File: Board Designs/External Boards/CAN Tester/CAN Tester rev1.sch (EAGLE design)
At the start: 25 parts, among them M1 Minifit, M2 Nanofit, U1 ISOLATED CAN TERMINAL, U2 TERMINATION_RESISTOR_JUMPER, U3 TEENSY_3.2_SIMPLE, U4 CHARACTER_LCD

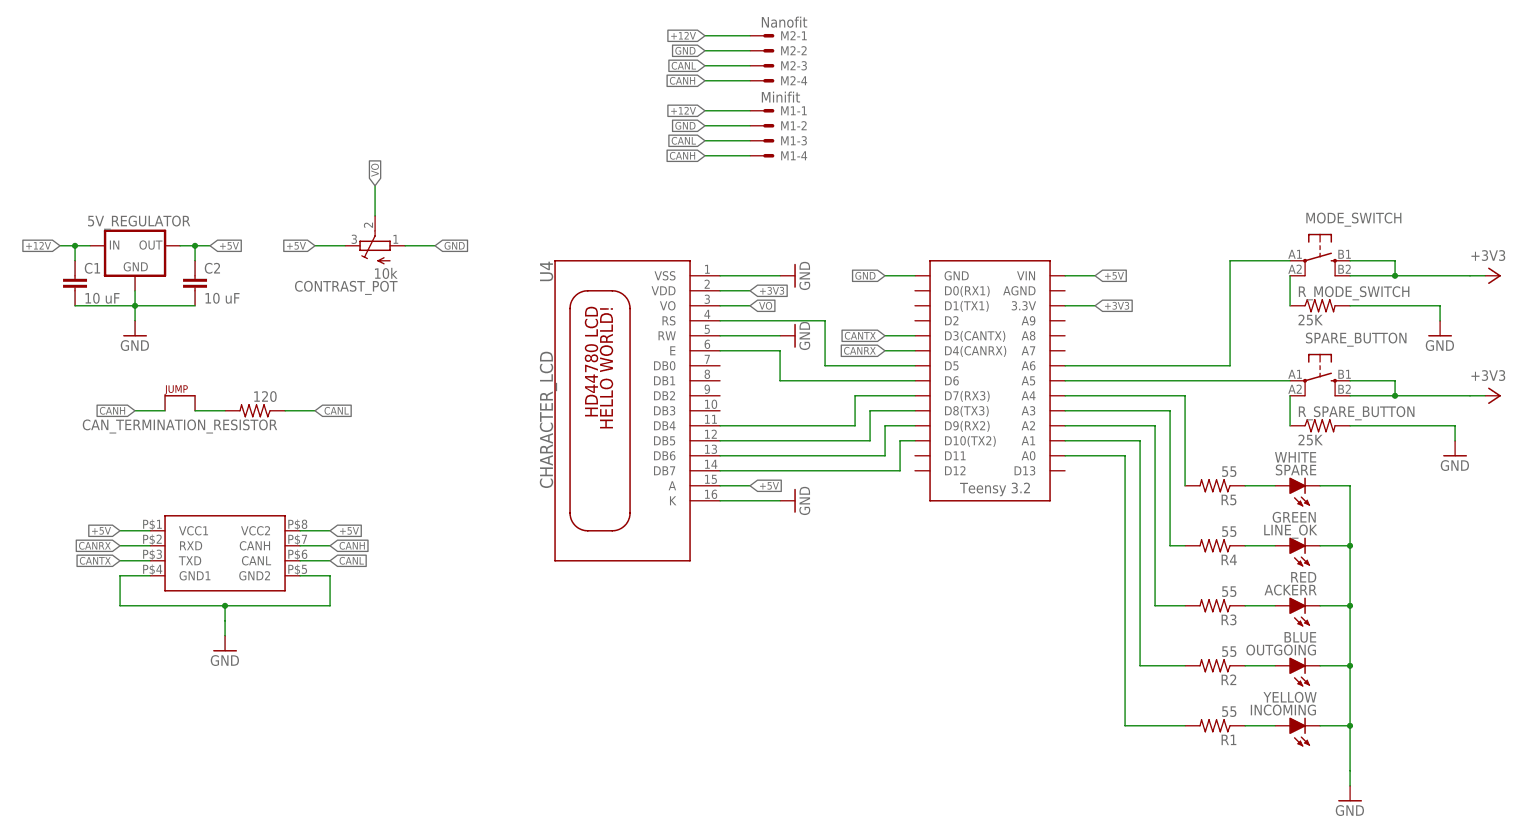
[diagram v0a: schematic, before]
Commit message: Moved the location of the can tester folder.
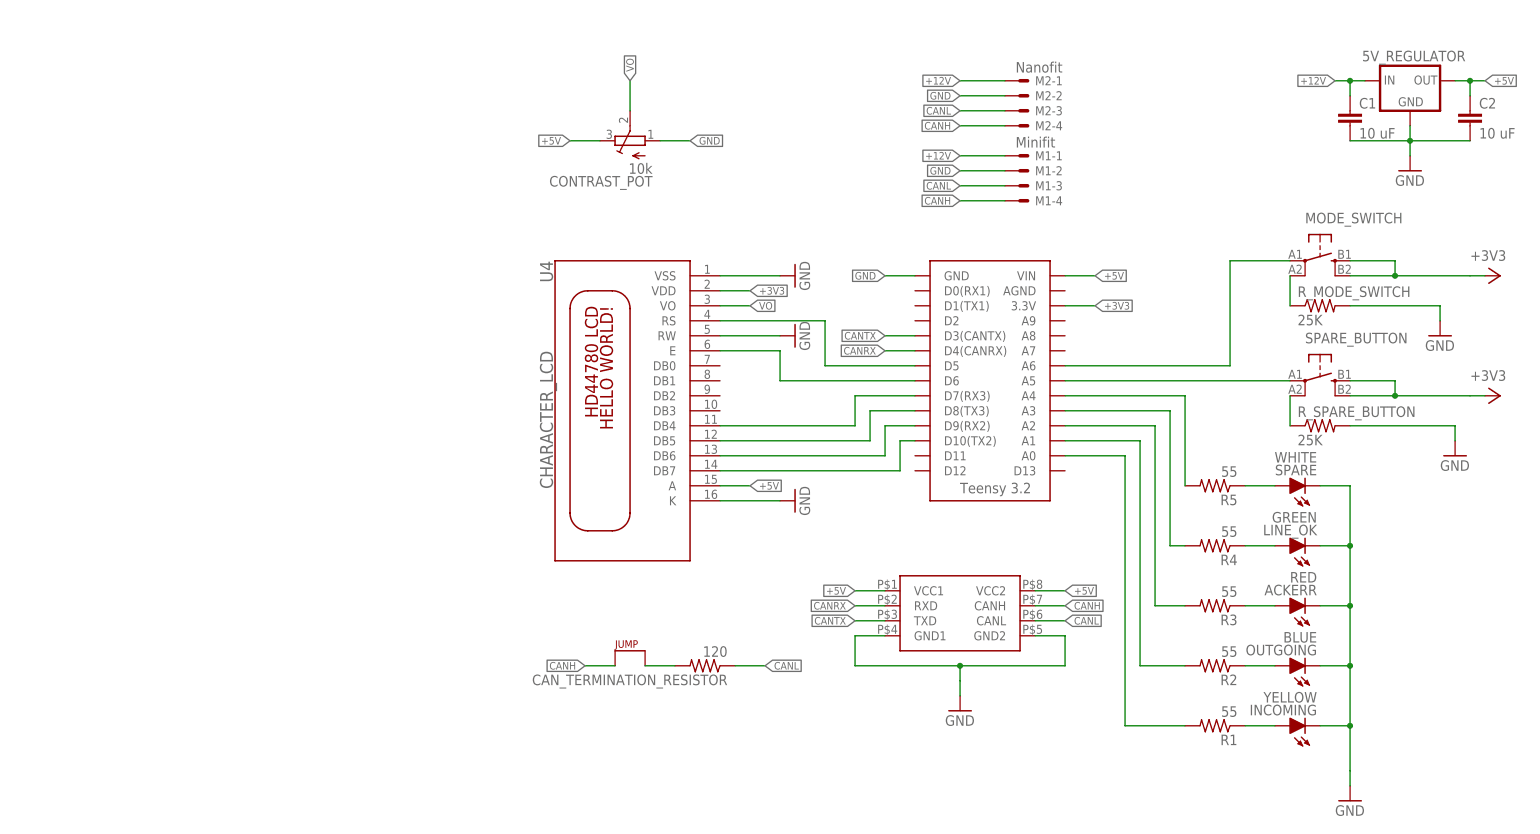
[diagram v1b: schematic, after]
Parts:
- U1: value ISOLATED CAN TERMINAL -> ISOLATED CAN TRANSCIEVER
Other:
- moved on the sheet: 5V_REGULATOR, C1, C2, CAN_TERMINATION_RESISTOR, CONTRAST_POT, M1-1, M1-2, M1-3, M1-4, M2-1, M2-2, M2-3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

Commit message: Verified schematic, but had to restart board
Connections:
- removed net N$15: R_MODE_SWITCH.2
- net GND: now also R_MODE_SWITCH.2
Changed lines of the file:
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@@
 <setting verticaltext="up"/>
 </settings>
-<grid distance="0.1" unitdist="inch" unit="inch" style="dots" multiple="1" display="yes" altdistance="0.01" altunitdist="inch" altunit="inch"/>
+<grid distance="0.1" unitdist="inch" unit="inch" style="lines" multiple="1" display="yes" altdistance="0.01" altunitdist="inch" altunit="inch"/>
 <layers>
 <layer number="1" name="Top" color="4" fill="1" visible="no" active="no"/>
@@
 </variantdefs>
 <classes>
-<class number="0" name="default" width="0" drill="0">
+<class number="0" name="default" width="0.762" drill="0">
+<clearance class="0" value="0.381"/>
 </class>
 </classes>
@@
 </segment>
 <segment>
-<pinref part="R_SPARE_BUTTON" gate="G$1" pin="2"/>
-<wire x1="167.64" y1="40.64" x2="185.42" y2="40.64" width="0.1524" layer="91"/>
-<pinref part="GND3" gate="1" pin="GND"/>
-<wire x1="185.42" y1="40.64" x2="185.42" y2="38.1" width="0.1524" layer="91"/>
-</segment>
-<segment>
-<pinref part="GND4" gate="1" pin="GND"/>
-<wire x1="182.88" y1="60.96" x2="182.88" y2="58.42" width="0.1524" layer="91"/>
-</segment>
-<segment>
 <pinref part="GND5" gate="1" pin="GND"/>
 <wire x1="101.6" y1="-5.08" x2="101.6" y2="-2.54" width="0.1524" layer="91"/>
@@
 <wire x1="109.22" y1="83.82" x2="101.6" y2="83.82" width="0.1524" layer="91"/>
 <label x="101.6" y="83.82" size="1.27" layer="95" rot="R180" xref="yes"/>
+</segment>
+<segment>
+<pinref part="R_SPARE_BUTTON" gate="G$1" pin="2"/>
+<pinref part="GND3" gate="1" pin="GND"/>
+<wire x1="167.64" y1="40.64" x2="185.42" y2="40.64" width="0.1524" layer="91"/>
+<wire x1="185.42" y1="40.64" x2="185.42" y2="38.1" width="0.1524" layer="91"/>
+</segment>
+<segment>
+<pinref part="GND4" gate="1" pin="GND"/>
+<wire x1="182.88" y1="58.42" x2="182.88" y2="60.96" width="0.1524" layer="91"/>
+<pinref part="R_MODE_SWITCH" gate="G$1" pin="2"/>
+<wire x1="182.88" y1="60.96" x2="167.64" y2="60.96" width="0.1524" layer="91"/>
 </segment>
 </net>
@@
 <pinref part="SPARE_BUTTON" gate="1" pin="P"/>
 <wire x1="119.38" y1="48.26" x2="157.48" y2="48.26" width="0.1524" layer="91"/>
-</segment>
-</net>
-<net name="N$12" class="0">
-<segment>
-<pinref part="SPARE_BUTTON" gate="1" pin="P1"/>
-<pinref part="R_SPARE_BUTTON" gate="G$1" pin="1"/>
-<wire x1="157.48" y1="45.72" x2="157.48" y2="40.64" width="0.1524" layer="91"/>
 </segment>
 </net>
@@
 <pinref part="MODE_SWITCH" gate="1" pin="P"/>
 <wire x1="147.32" y1="68.58" x2="157.48" y2="68.58" width="0.1524" layer="91"/>
-</segment>
-</net>
-<net name="N$14" class="0">
-<segment>
-<pinref part="MODE_SWITCH" gate="1" pin="P1"/>
-<pinref part="R_MODE_SWITCH" gate="G$1" pin="1"/>
-<wire x1="157.48" y1="66.04" x2="157.48" y2="60.96" width="0.1524" layer="91"/>
-</segment>
-</net>
-<net name="N$15" class="0">
-<segment>
-<pinref part="R_MODE_SWITCH" gate="G$1" pin="2"/>
-<wire x1="167.64" y1="60.96" x2="182.88" y2="60.96" width="0.1524" layer="91"/>
 </segment>
 </net>
@@
 </segment>
 </net>
+<net name="N$12" class="0">
+<segment>
+<pinref part="MODE_SWITCH" gate="1" pin="P1"/>
+<pinref part="R_MODE_SWITCH" gate="G$1" pin="1"/>
+<wire x1="157.48" y1="66.04" x2="157.48" y2="60.96" width="0.1524" layer="91"/>
+</segment>
+</net>
+<net name="N$14" class="0">
+<segment>
+<pinref part="SPARE_BUTTON" gate="1" pin="P1"/>
+<pinref part="R_SPARE_BUTTON" gate="G$1" pin="1"/>
+<wire x1="157.48" y1="45.72" x2="157.48" y2="40.64" width="0.1524" layer="91"/>
+</segment>
+</net>

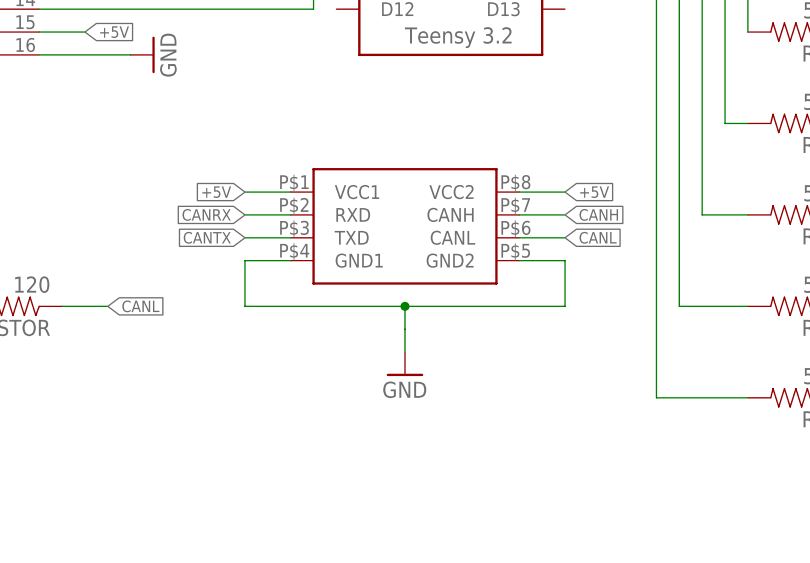
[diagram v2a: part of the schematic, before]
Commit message: Finished CAN_Tester Board
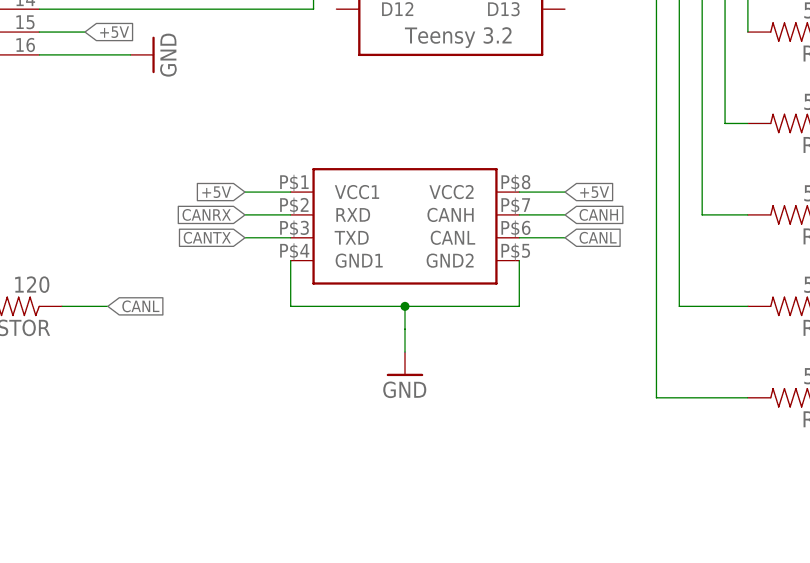
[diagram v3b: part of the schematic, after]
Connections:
- removed net VSS: U4.VSS
- net GND: now also U4.VSS
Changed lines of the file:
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@@
 <wire x1="182.88" y1="60.96" x2="167.64" y2="60.96" width="0.1524" layer="91"/>
+</segment>
+<segment>
+<pinref part="GND8" gate="1" pin="GND"/>
+<wire x1="60.96" y1="66.04" x2="71.12" y2="66.04" width="0.1524" layer="91"/>
+<pinref part="U4" gate="G$1" pin="VSS"/>
 </segment>
 </net>
@@
 <segment>
 <pinref part="U1" gate="G$1" pin="GND2"/>
-<wire x1="114.3" y1="5.08" x2="119.38" y2="5.08" width="0.1524" layer="91"/>
-<wire x1="119.38" y1="5.08" x2="119.38" y2="0" width="0.1524" layer="91"/>
+<wire x1="114.3" y1="5.08" x2="114.3" y2="0" width="0.1524" layer="91"/>
 <pinref part="U1" gate="G$1" pin="GND1"/>
-<wire x1="88.9" y1="5.08" x2="83.82" y2="5.08" width="0.1524" layer="91"/>
-<wire x1="83.82" y1="5.08" x2="83.82" y2="0" width="0.1524" layer="91"/>
-<wire x1="83.82" y1="0" x2="101.6" y2="0" width="0.1524" layer="91"/>
+<wire x1="88.9" y1="5.08" x2="88.9" y2="0" width="0.1524" layer="91"/>
+<wire x1="88.9" y1="0" x2="101.6" y2="0" width="0.1524" layer="91"/>
 <wire x1="101.6" y1="0" x2="101.6" y2="-2.54" width="0.1524" layer="91"/>
-<wire x1="119.38" y1="0" x2="101.6" y2="0" width="0.1524" layer="91"/>
+<wire x1="114.3" y1="0" x2="101.6" y2="0" width="0.1524" layer="91"/>
 <junction x="101.6" y="0"/>
 </segment>
@@
 <wire x1="60.96" y1="60.96" x2="66.04" y2="60.96" width="0.1524" layer="91"/>
 <label x="66.04" y="60.96" size="1.27" layer="95" xref="yes"/>
-</segment>
-</net>
-<net name="VSS" class="0">
-<segment>
-<pinref part="GND8" gate="1" pin="GND"/>
-<wire x1="60.96" y1="66.04" x2="71.12" y2="66.04" width="0.1524" layer="91"/>
-<pinref part="U4" gate="G$1" pin="VSS"/>
 </segment>
 </net>
@@
 </sheet>
 </sheets>
+<errors>
+</errors>
 </schematic>
 </drawing>

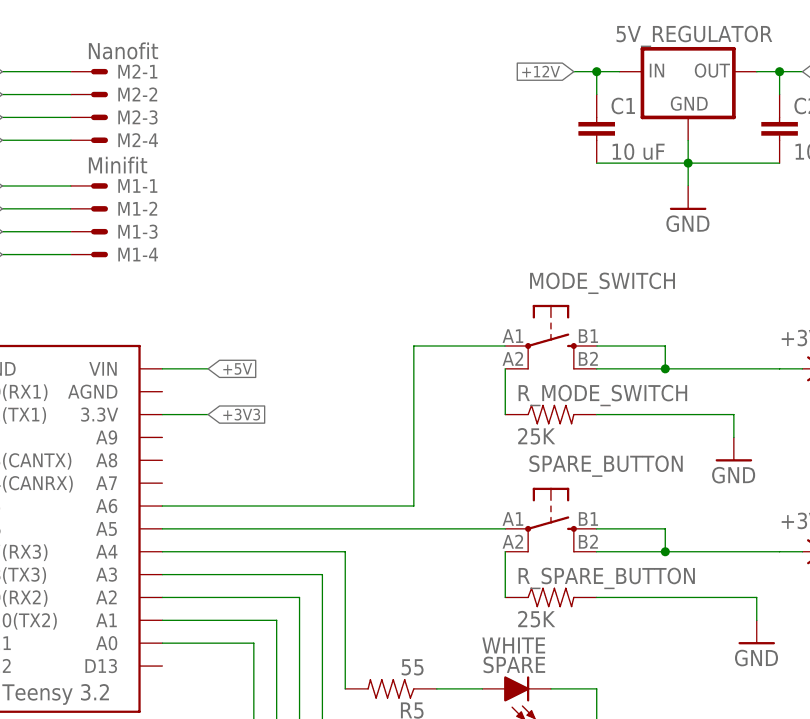
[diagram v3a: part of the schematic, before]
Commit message: Added anothe rminifit and nano fit. Changed some components to through hole.
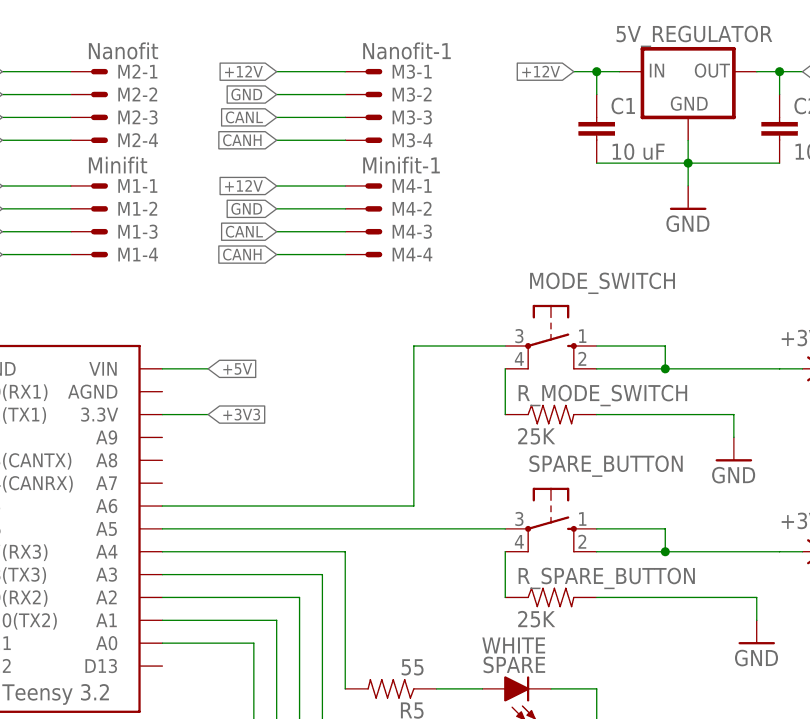
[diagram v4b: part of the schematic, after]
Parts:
- added M3: Nanofit-1, HyTechDevices:CONNECTOR-4NANO-FIT-VERTICAL-4
- added M4: Minifit-1, HyTechDevices:CONNECTOR-4
- M1: device HyTechDevices:CONNECTOR-4DURACLIK_RIGHT_ANGLE-4 -> HyTechDevices:CONNECTOR-4
- M2: device HyTechDevices:CONNECTOR-4NANO-FIT_RIGHT_ANGLE-4-SURFACE -> HyTechDevices:CONNECTOR-4NANO-FIT-VERTICAL-4
- MODE_SWITCH, SPARE_BUTTON: device HyTechDevices:BTN_10-XXSMD -> HyTechDevices:BTN_10-XX
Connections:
- net +12V: now also M3-1.S, M4-1.S
- net CANH: now also M3-4.S, M4-4.S
- net CANL: now also M3-3.S, M4-3.S
- net GND: now also M3-2.S, M4-2.S

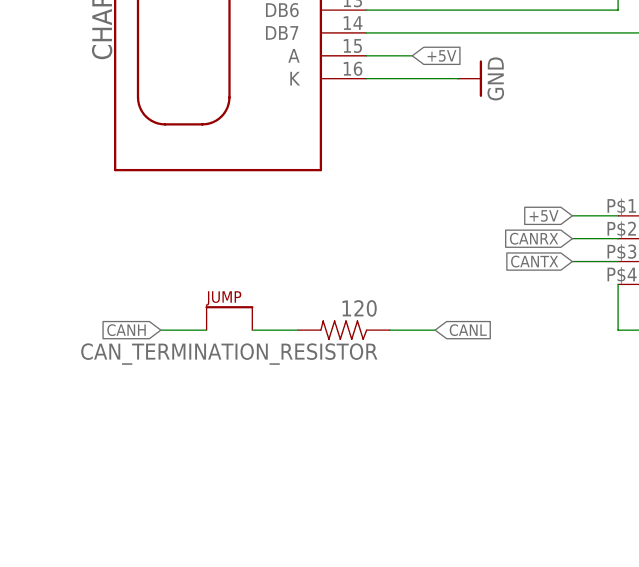
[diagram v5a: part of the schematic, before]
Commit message: Almost done with CAN tester board, just changed the jumper package
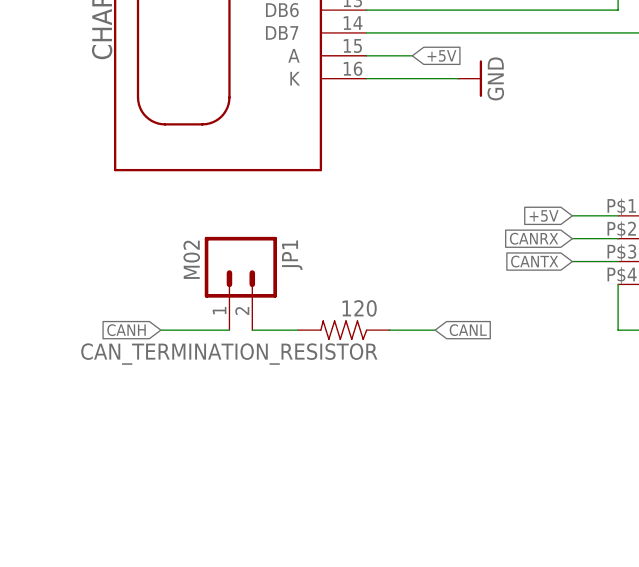
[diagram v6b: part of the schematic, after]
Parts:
- removed U2: TERMINATION_RESISTOR_JUMPER, HyTechDevices:JUMPER
- added JP1: M02, HyTechDevices:M02
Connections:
- net CANH: now also JP1.1; no longer U2.P$1
- net CANL: now also JP1.2; no longer U2.P$2
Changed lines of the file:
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@@
 <part name="MODE_SWITCH" library="HyTechDevices" deviceset="BTN_10-XX" device=""/>
 <part name="SPARE_BUTTON" library="HyTechDevices" deviceset="BTN_10-XX" device=""/>
-<part name="U2" library="HyTechDevices" deviceset="JUMPER" device="" value="TERMINATION_RESISTOR_JUMPER"/>
 <part name="CAN_TERMINATION_RESISTOR" library="HyTechDevices" deviceset="RESISTOR" device="0805-RES" value="120"/>
 <part name="R1" library="HyTechDevices" deviceset="RESISTOR" device="0805-RES" value="55"/>
@@
 <part name="M3" library="HyTechDevices" deviceset="CONNECTOR-4" device="NANO-FIT-VERTICAL-4" value="Nanofit-1"/>
 <part name="M4" library="HyTechDevices" deviceset="CONNECTOR-4" device="" value="Minifit-1"/>
+<part name="JP1" library="HyTechDevices" deviceset="M02" device=""/>
 </parts>
 <sheets>
@@
 <instance part="MODE_SWITCH" gate="1" x="162.56" y="68.58" rot="R270"/>
 <instance part="SPARE_BUTTON" gate="1" x="162.56" y="48.26" rot="R270"/>
-<instance part="U2" gate="G$1" x="43.18" y="2.54"/>
 <instance part="CAN_TERMINATION_RESISTOR" gate="G$1" x="58.42" y="0" rot="R180"/>
 <instance part="R1" gate="G$1" x="144.78" y="-10.16" rot="R180"/>
@@
 <instance part="M4" gate="-3" x="142.24" y="81.28"/>
 <instance part="M4" gate="-4" x="142.24" y="78.74"/>
+<instance part="JP1" gate="G$1" x="45.72" y="7.62" rot="R270"/>
 </instances>
 <busses>
@@
 <segment>
 <pinref part="CAN_TERMINATION_RESISTOR" gate="G$1" pin="1"/>
-<pinref part="U2" gate="G$1" pin="P$2"/>
 <pinref part="CAN_TERMINATION_RESISTOR" gate="G$1" pin="2"/>
 <wire x1="53.34" y1="0" x2="48.26" y2="0" width="0.1524" layer="91"/>
 <wire x1="63.5" y1="0" x2="68.58" y2="0" width="0.1524" layer="91"/>
 <label x="68.58" y="0" size="1.27" layer="95" xref="yes"/>
+<pinref part="JP1" gate="G$1" pin="2"/>
 </segment>
 <segment>
@@
 </segment>
 <segment>
-<pinref part="U2" gate="G$1" pin="P$1"/>
-<wire x1="43.18" y1="0" x2="38.1" y2="0" width="0.1524" layer="91"/>
+<wire x1="45.72" y1="0" x2="38.1" y2="0" width="0.1524" layer="91"/>
 <label x="38.1" y="0" size="1.27" layer="95" rot="R180" xref="yes"/>
-</segment>
-<segment>
+<pinref part="JP1" gate="G$1" pin="1"/>
+</segment>
+<segment>
